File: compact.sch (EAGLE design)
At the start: 38 parts, among them J3 AVX_6-PIN_009159006061916, J4 CORTEX_DEBUG_PTH, J5 10118194-0001LF, U1 STM32F103C8T6, U2 CJT1117-3.3-SOT223

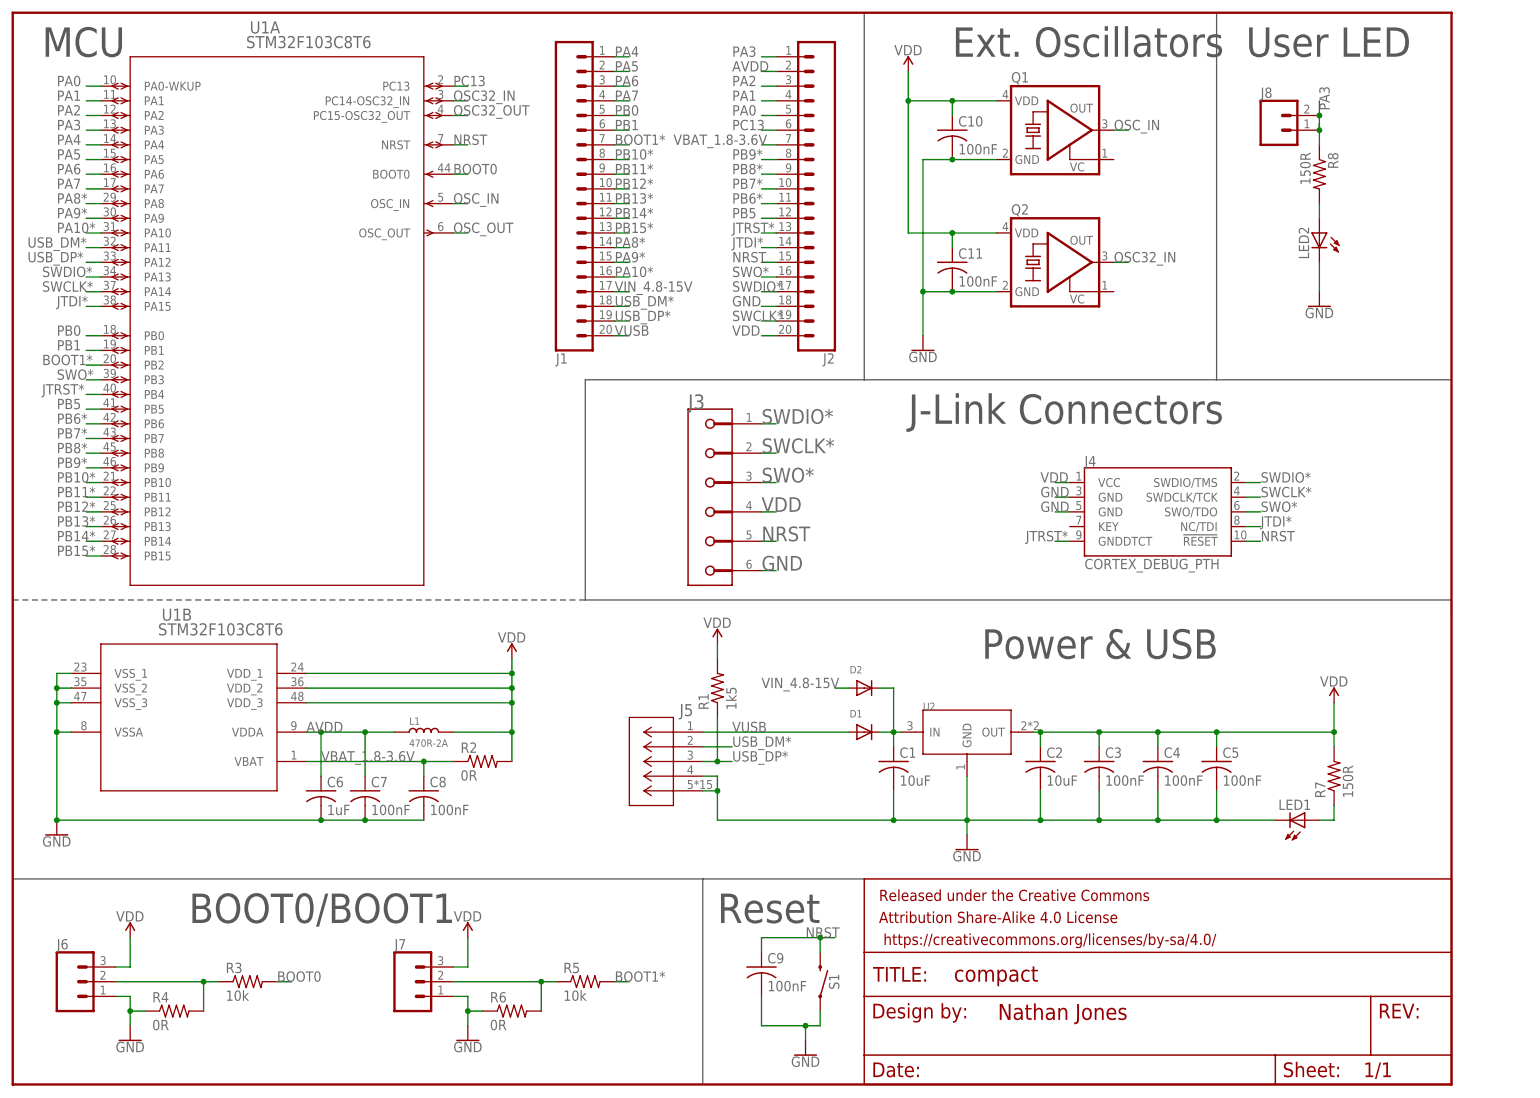
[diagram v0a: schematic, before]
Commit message: Changed USB connector to mini-B. Change pin labels on the silkscreen to be more readable.
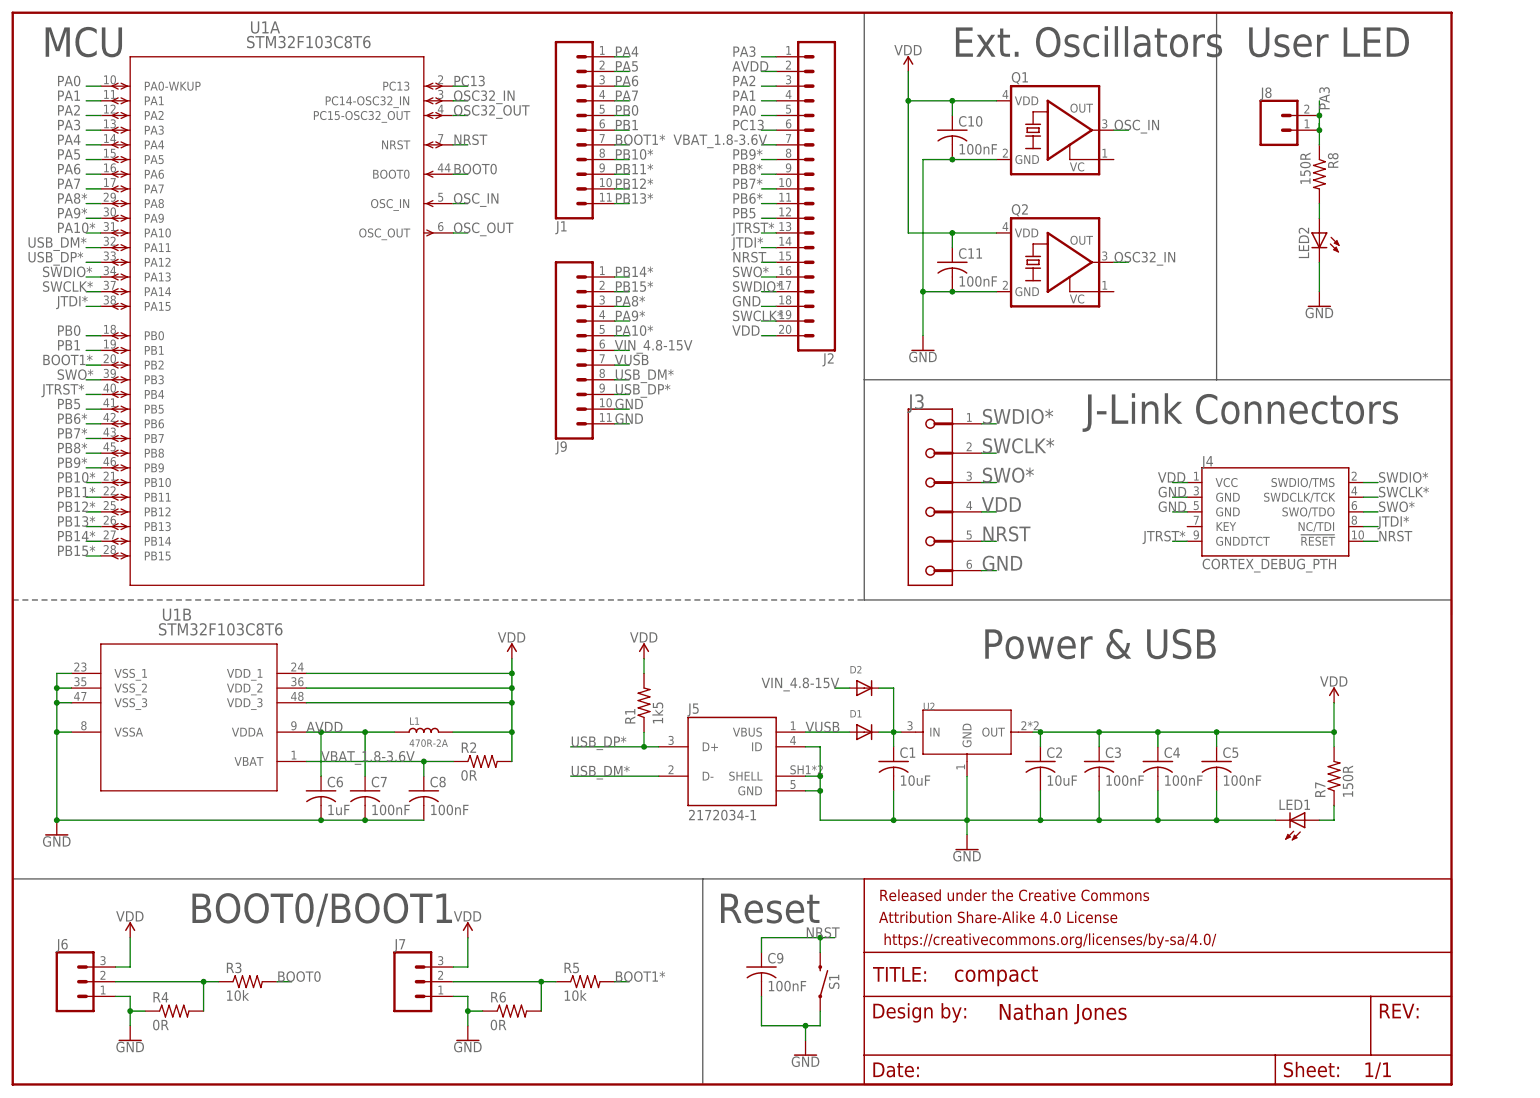
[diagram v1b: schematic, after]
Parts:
- added J9: (no value), SparkFun-Connectors:CONN_111X11_NO_SILK
- J1: device SparkFun-Connectors:CONN_20NOSILK -> SparkFun-Connectors:CONN_111X11_NO_SILK
- J5: value 10118194-0001LF -> 2172034-1; device USB-micro-B_Amphenol_10118194-0001LF:10118194-0001LF -> USB-mini-B_TE_2172034-1:2172034-1
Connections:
- net GND: now also J5.GND, J5.ID, J5.SHELL, J9.10, J9.11; no longer J5.4, J5.5
- net PA10*: now also J9.5; no longer J1.16
- net PA8*: now also J9.3; no longer J1.14
- net PA9*: now also J9.4; no longer J1.15
- net PB14*: now also J9.1; no longer J1.12
- net PB15*: now also J9.2; no longer J1.13
- net USB_DM*: now also J5.D-, J9.8; no longer J1.18, J5.2
- net USB_DP*: now also J5.D+, J9.9; no longer J1.19, J5.3
- net VIN_4.8-15V: now also J9.6; no longer J1.17
- net VUSB: now also J5.VBUS, J9.7; no longer J1.20, J5.1
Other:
- moved on the sheet: J3, J4, R1
